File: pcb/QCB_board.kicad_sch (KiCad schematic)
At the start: 27 parts, among them J2 39-29-3086, J4 Conn_01x04_Socket

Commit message: Schematic design
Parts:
- removed C10, C11, C13, C14, C4, C5, C7, C8: 100n, Capacitor_SMD:C_0603_1608Metric_Pad1.08x0.95mm_HandSolder, symbol Device:C
- removed C12, C15, C6, C9: 10u, Capacitor_SMD:C_1206_3216Metric_Pad1.33x1.80mm_HandSolder, symbol Device:C
- removed D1: SMF5.0CA, Diode_SMD:D_SMF, symbol Diode:SMF5V0A
- removed D10: ESD5Z3.3T1G, Diode_SMD:D_SOD-523, symbol Diode:ESD5Zxx
- removed F1, F2: Polyfuse, Fuse:Fuse_1206_3216Metric_Pad1.42x1.75mm_HandSolder, symbol Device:Polyfuse
- removed J2: 39-29-3086, Connector_Molex:Molex_Mini-Fit_Jr_5566-08A_2x04_P4.20mm_Vertical, symbol SamacSys_Parts:39-29-3086
- removed J4: Conn_01x04_Socket, Connector_JST:JST_PH_B4B-PH-K_1x04_P2.00mm_Vertical, symbol Connector:Conn_01x04_Socket
- removed L1, L2: LQH32PN101MN0L, Inductor_SMD:L_1210_3225Metric, symbol Device:L
- removed TP3, TP4: TestPoint, TestPoint:TestPoint_Pad_D1.0mm, symbol Connector:TestPoint
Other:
- added sheet PWR (pwr.kicad_sch)

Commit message: More schematic
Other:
- sheet PWR ports: added +12V, +3.3V, +5V, +5Vsb, -12V; removed none
- sheet USB_Switch ports: added D1+, D1-, D2+, D2-, D3+, D3-, D4+, D4-; removed none
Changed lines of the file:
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@@
-			)
-		)
-		(pin "+3.3V" input
-			(at 146.05 182.88 0)
-			(effects
-				(font
-					(size 1.27 1.27)
-				)
-				(justify right)
-			)
-		)
-		(pin "+5V" input
-			(at 146.05 185.42 0)
-			(effects
-				(font
-					(size 1.27 1.27)
-				)
-				(justify right)
 			)
 		)
@@
 		(pin "VUSB" input
 			(at 146.05 195.58 0)
+			(effects
+				(font
+					(size 1.27 1.27)
+				)
+				(justify right)
+			)
+		)
+		(pin "+3.3V" input
+			(at 146.05 185.42 0)
+			(effects
+				(font
+					(size 1.27 1.27)
+				)
+				(justify right)
+			)
+		)
+		(pin "+5V" input
+			(at 146.05 182.88 0)
 			(effects
 				(font
@@
 	)
 	(sheet
-		(at 163.83 175.26)
-		(size 17.78 45.72)
+		(at 124.46 128.27)
+		(size 17.78 26.67)
 		(exclude_from_sim no)
 		(in_bom yes)
@@
 		)
 		(property "Sheetname" "USB_Switch"
-			(at 163.83 174.5484 0)
+			(at 124.46 127.5584 0)
 			(effects
 				(font
@@
 		)
 		(property "Sheetfile" "usb_switch.kicad_sch"
-			(at 163.83 221.5646 0)
+			(at 124.46 155.5246 0)
 			(effects
 				(font
@@
 				)
 				(justify left top)
+			)
+		)
+		(pin "D1+" input
+			(at 142.24 130.81 0)
+			(effects
+				(font
+					(size 1.27 1.27)
+				)
+				(justify right)
+			)
+		)
+		(pin "D1-" input
+			(at 142.24 133.35 0)
+			(effects
+				(font
+					(size 1.27 1.27)
+				)
+				(justify right)
+			)
+		)
+		(pin "D2+" input
+			(at 142.24 137.16 0)
+			(effects
+				(font
+					(size 1.27 1.27)
+				)
+				(justify right)
+			)
+		)
+		(pin "D2-" input
+			(at 142.24 139.7 0)
+			(effects
+				(font
+					(size 1.27 1.27)
+				)
+				(justify right)
+			)
+		)
+		(pin "D3+" input
+			(at 142.24 143.51 0)
+			(effects
+				(font
+					(size 1.27 1.27)
+				)
+				(justify right)
+			)
+		)
+		(pin "D3-" input
+			(at 142.24 146.05 0)
+			(effects
+				(font
+					(size 1.27 1.27)
+				)
+				(justify right)
+			)
+		)
+		(pin "D4+" input
+			(at 142.24 149.86 0)
+			(effects
+				(font
+					(size 1.27 1.27)
+				)
+				(justify right)
+			)
+		)
+		(pin "D4-" input
+			(at 142.24 152.4 0)
+			(effects
+				(font
+					(size 1.27 1.27)
+				)
+				(justify right)
 			)
 		)
@@
 	)
 	(sheet
-		(at 308.61 151.13)
-		(size 12.7 35.56)
+		(at 195.58 135.89)
+		(size 12.7 15.24)
 		(exclude_from_sim no)
 		(in_bom yes)
@@
 		)
 		(property "Sheetname" "PWR"
-			(at 308.61 150.4184 0)
+			(at 195.58 135.1784 0)
 			(effects
 				(font
@@
 		)
 		(property "Sheetfile" "pwr.kicad_sch"
-			(at 308.61 187.2746 0)
+			(at 195.58 151.7146 0)
 			(effects
 				(font
@@
 			)
 		)
+		(pin "+3.3V" input
+			(at 195.58 146.05 180)
+			(effects
+				(font
+					(size 1.27 1.27)
+				)
+				(justify left)
+			)
+		)
+		(pin "+5V" input
+			(at 195.58 143.51 180)
+			(effects
+				(font
+					(size 1.27 1.27)
+				)
+				(justify left)
+			)
+		)
+		(pin "+5Vsb" input
+			(at 195.58 148.59 180)
+			(effects
+				(font
+					(size 1.27 1.27)
+				)
+				(justify left)
+			)
+		)
+		(pin "+12V" input
+			(at 195.58 138.43 180)
+			(effects
+				(font
+					(size 1.27 1.27)
+				)
+				(justify left)
+			)
+		)
+		(pin "-12V" input
+			(at 195.58 140.97 180)
+			(effects
+				(font
+					(size 1.27 1.27)
+				)
+				(justify left)
+			)
+		)

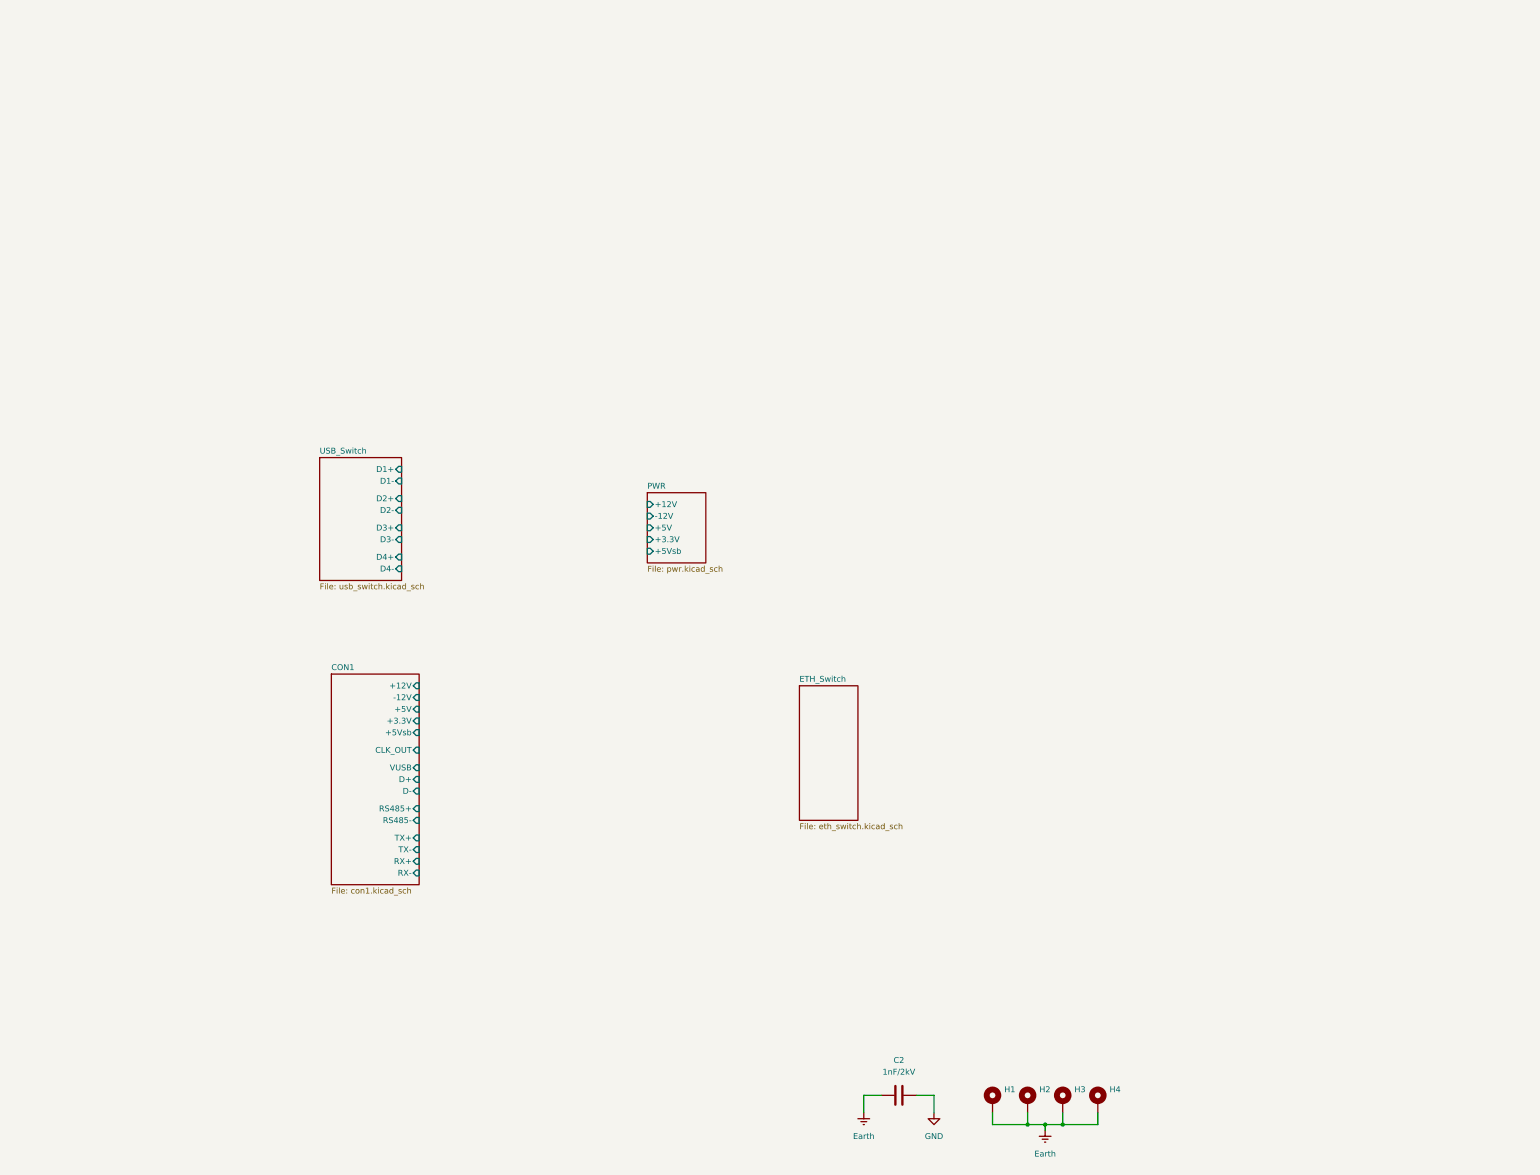
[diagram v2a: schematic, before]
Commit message: Sch complete, starting pcb
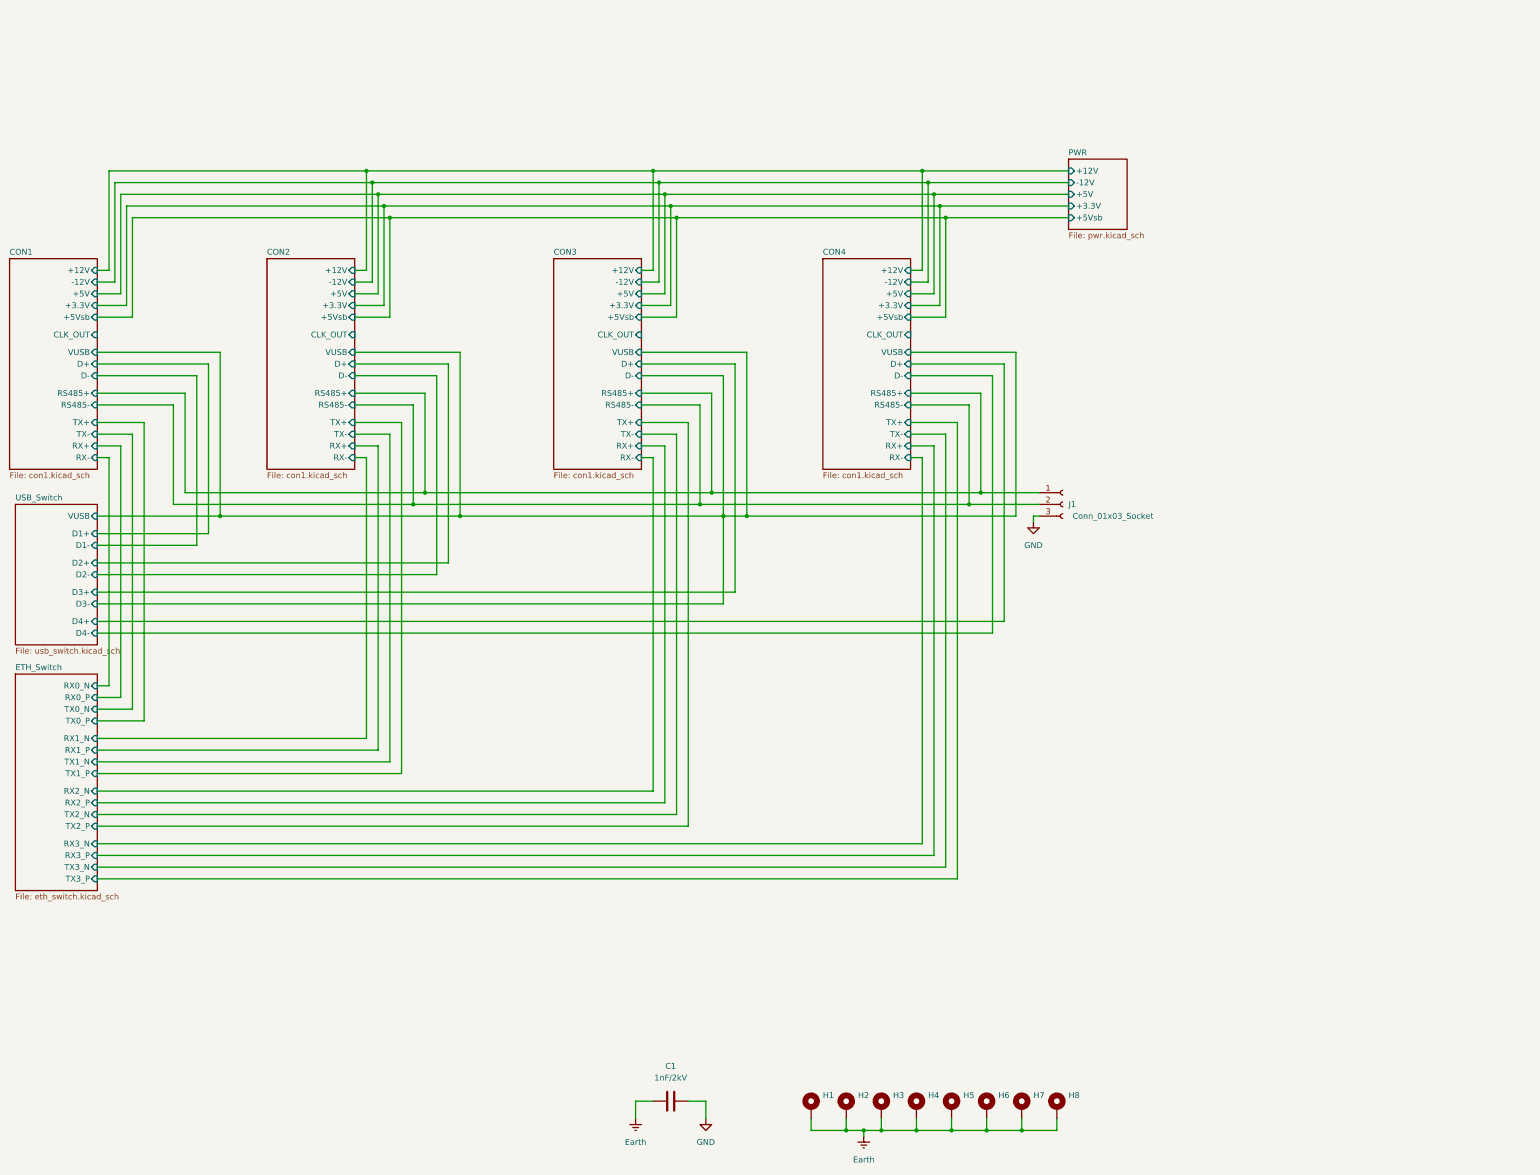
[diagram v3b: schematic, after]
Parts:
- added H5, H6, H7, H8: MountingHole_Pad, MountingHole:MountingHole_2.7mm_M2.5_DIN965_Pad, symbol Mechanical:MountingHole_Pad
- added J1: Conn_01x03_Socket, Connector_JST:JST_PH_B3B-PH-K_1x03_P2.00mm_Vertical, symbol Connector:Conn_01x03_Socket
- renumbered C2 to C1
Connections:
- net CON1/RS485+: now also J1.1 (Pin_1)
- net CON1/RS485-: now also J1.2 (Pin_2)
- net Earth: now also H5.1, H6.1, H7.1, H8.1
- net GND: now also J1.3 (Pin_3)
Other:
- added sheet CON2 (con1.kicad_sch)
- added sheet CON3 (con1.kicad_sch)
- added sheet CON4 (con1.kicad_sch)
- sheet ETH_Switch ports: added RX0_N, RX0_P, RX1_N, RX1_P, RX2_N, RX2_P, RX3_N, RX3_P, TX0_N, TX0_P, TX1_N, TX1_P, TX2_N, TX2_P, TX3_N, TX3_P; removed none
- sheet USB_Switch ports: added VUSB; removed none
- moved on the sheet: C1, H1, H2, H3, H4

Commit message: Routing
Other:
- sheet CON1 ports: added +12V_PWR, +3.3V_PWR, +5V_PWR, -12V_PWR; removed +12V, +3.3V, +5V, -12V
- sheet CON2 ports: added +12V_PWR, +3.3V_PWR, +5V_PWR, -12V_PWR; removed +12V, +3.3V, +5V, -12V
- sheet CON3 ports: added +12V_PWR, +3.3V_PWR, +5V_PWR, -12V_PWR; removed +12V, +3.3V, +5V, -12V
- sheet CON4 ports: added +12V_PWR, +3.3V_PWR, +5V_PWR, -12V_PWR; removed +12V, +3.3V, +5V, -12V
- sheet PWR ports: added +12V_PWR, +3.3V_PWR, +5V_PWR, -12V_PWR; removed +12V, +3.3V, +5V, -12V
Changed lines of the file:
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@@
 	)
 	(junction
-		(at 212.09 140.97)
-		(diameter 0)
-		(color 0 0 0 0)
-	)
-	(junction
 		(at 147.32 135.89)
 		(diameter 0)
@@
 	(wire
 		(pts
-			(xy 212.09 140.97) (xy 212.09 160.02)
-		)
-		(stroke
-			(width 0)
-			(type default)
-		)
-	)
-	(wire
-		(pts
-			(xy 212.09 140.97) (xy 217.17 140.97)
+			(xy 212.09 110.49) (xy 212.09 160.02)
 		)
 		(stroke
@@
 	(wire
 		(pts
-			(xy 154.94 140.97) (xy 212.09 140.97)
+			(xy 154.94 140.97) (xy 217.17 140.97)
 		)
 		(stroke
@@
 	(wire
 		(pts
-			(xy 212.09 110.49) (xy 212.09 140.97)
-		)
-		(stroke
-			(width 0)
-			(type default)
-		)
-	)
-	(wire
-		(pts
 			(xy 214.63 107.95) (xy 194.31 107.95)
 		)
@@
 			)
 		)
-		(pin "+12V" input
+		(pin "+12V_PWR" input
 			(at 76.2 87.63 0)
 			(effects
@@
 			)
 		)
-		(pin "-12V" input
+		(pin "-12V_PWR" input
 			(at 76.2 90.17 0)
 			(effects
@@
 			)
 		)
-		(pin "+3.3V" input
+		(pin "+3.3V_PWR" input
 			(at 76.2 95.25 0)
 			(effects
@@
 			)
 		)
-		(pin "+5V" input
+		(pin "+5V_PWR" input
 			(at 76.2 92.71 0)
 			(effects
@@
 			)
 		)
-		(pin "+12V" input
+		(pin "+12V_PWR" input
 			(at 132.08 87.63 0)
 			(effects
@@
 			)
 		)
-		(pin "-12V" input
+		(pin "-12V_PWR" input
 			(at 132.08 90.17 0)
 			(effects
@@
 			)
 		)
-		(pin "+3.3V" input
+		(pin "+3.3V_PWR" input
 			(at 132.08 95.25 0)
 			(effects
@@
 			)
 		)
-		(pin "+5V" input
+		(pin "+5V_PWR" input
 			(at 132.08 92.71 0)
 			(effects
@@
 			)
 		)
-		(pin "+12V" input
+		(pin "+12V_PWR" input
 			(at 252.73 87.63 0)
 			(effects
@@
 			)
 		)
-		(pin "-12V" input
+		(pin "-12V_PWR" input
 			(at 252.73 90.17 0)
 			(effects
@@
 			)
 		)
-		(pin "+3.3V" input
+		(pin "+3.3V_PWR" input
 			(at 252.73 95.25 0)
 			(effects
@@
 			)
 		)
-		(pin "+5V" input
+		(pin "+5V_PWR" input
 			(at 252.73 92.71 0)
 			(effects
@@
 			)
 		)
-		(pin "+12V" input
+		(pin "+12V_PWR" input
 			(at 194.31 87.63 0)
 			(effects
@@
 			)
 		)
-		(pin "-12V" input
+		(pin "-12V_PWR" input
 			(at 194.31 90.17 0)
 			(effects
@@
 			)
 		)
-		(pin "+3.3V" input
+		(pin "+3.3V_PWR" input
 			(at 194.31 95.25 0)
 			(effects
@@
 			)
 		)
-		(pin "+5V" input
+		(pin "+5V_PWR" input
 			(at 194.31 92.71 0)
 			(effects
@@
 			)
 		)
-		(pin "+3.3V" input
+		(pin "+3.3V_PWR" input
 			(at 287.02 73.66 180)
 			(effects
@@
 			)
 		)
-		(pin "+5V" input
+		(pin "+5V_PWR" input
 			(at 287.02 71.12 180)
 			(effects
@@
 			)
 		)
-		(pin "+12V" input
+		(pin "+12V_PWR" input
 			(at 287.02 66.04 180)
 			(effects
@@
 			)
 		)
-		(pin "-12V" input
+		(pin "-12V_PWR" input
 			(at 287.02 68.58 180)
 			(effects
